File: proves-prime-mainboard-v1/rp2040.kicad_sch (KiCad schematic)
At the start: 38 parts, among them IC1 RP2040_QFN56, IC2 AZ1117CH-3.3TRG1, SW1 KMR2, SW2 KMR2, SW3 SW_SPDT, U1 W25Q128JV, Y1 12MHZ

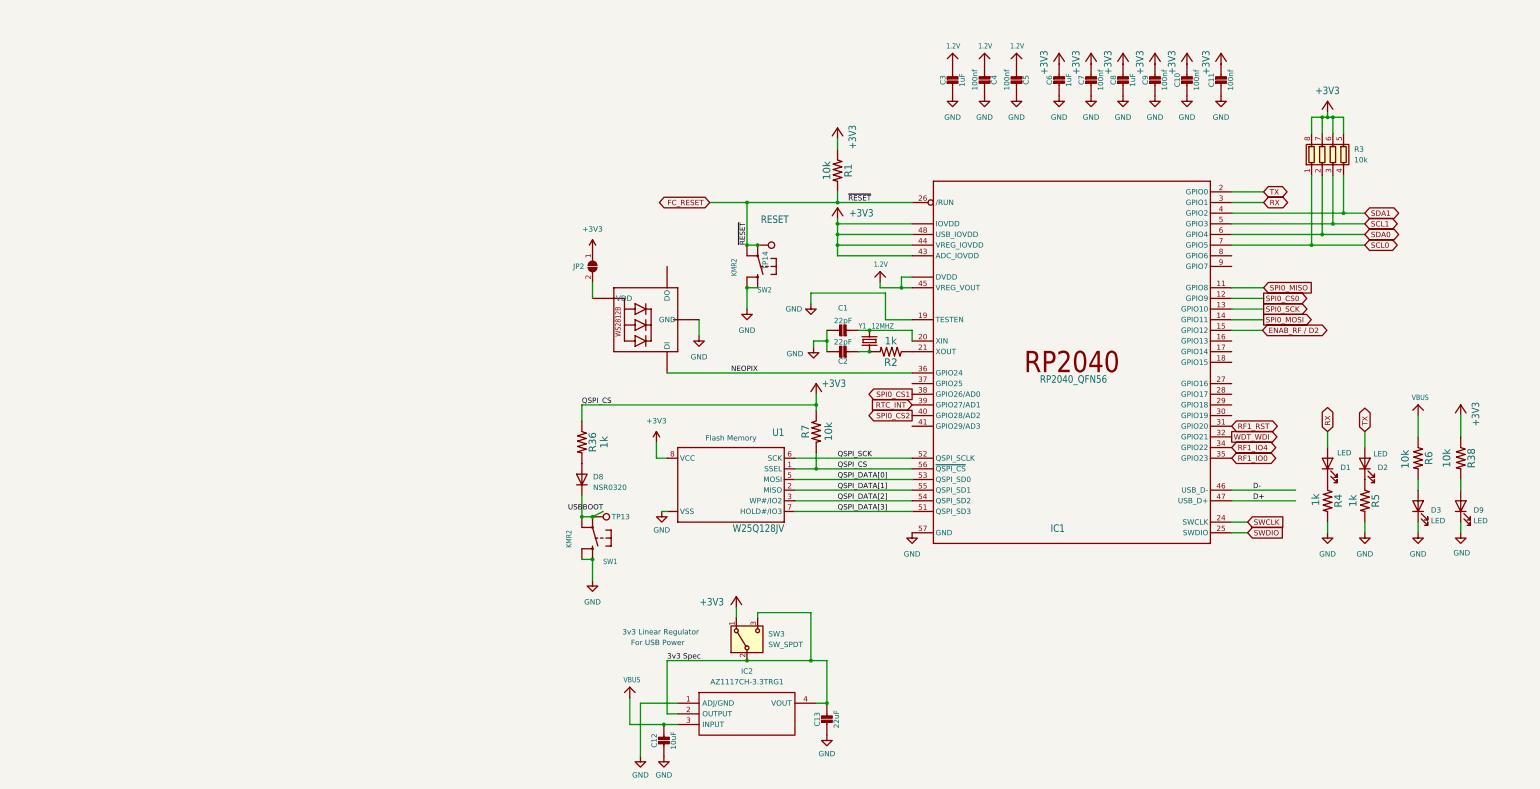
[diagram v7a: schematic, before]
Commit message: Removed RP2040
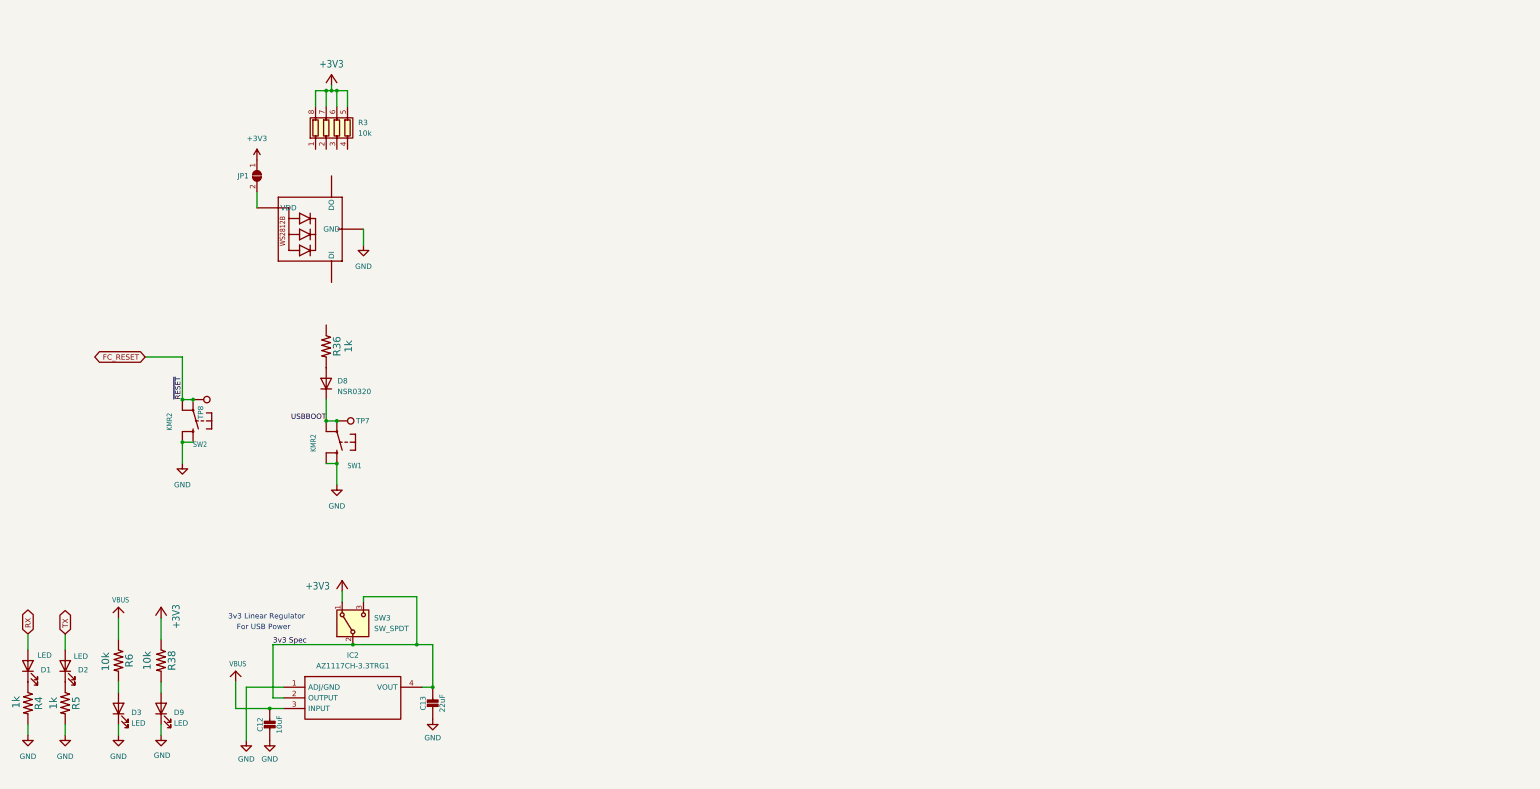
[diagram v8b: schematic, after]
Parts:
- removed C1, C2: 22pF, Capacitor_SMD:C_0402_1005Metric, symbol Adafruit ItsyBitsy RP2040-eagle-import:CAP_CERAMIC_0402NO
- removed C10, C11, C4, C5, C7, C9: 100nf, Capacitor_SMD:C_0402_1005Metric, symbol Adafruit ItsyBitsy RP2040-eagle-import:CAP_CERAMIC_0402NO
- removed C3, C6, C8: 1uF, Capacitor_SMD:C_0603_1608Metric, symbol Adafruit ItsyBitsy RP2040-eagle-import:CAP_CERAMIC_0603MP
- removed IC1: RP2040_QFN56, Package_DFN_QFN:QFN-56-1EP_7x7mm_P0.4mm_EP3.2x3.2mm_ThermalVias, symbol Adafruit ItsyBitsy RP2040-eagle-import:RP2040_QFN56
- removed JP2: SolderJumper_2_Open, Jumper:SolderJumper-2_P1.3mm_Open_RoundedPad1.0x1.5mm, symbol Jumper:SolderJumper_2_Open
- removed R1, R7: 10k, Resistor_SMD:R_0603_1608Metric, symbol mainboard:RESISTOR0603
- removed R2: 1k, Resistor_SMD:R_0402_1005Metric, symbol mainboard:RESISTOR0603
- removed TP13: USBBOOT, TestPoint:TestPoint_Loop_D1.80mm_Drill1.0mm_Beaded, symbol Connector:TestPoint
- removed TP14: RESET, TestPoint:TestPoint_Loop_D1.80mm_Drill1.0mm_Beaded, symbol Connector:TestPoint
- removed U1: W25Q128JV, Package_SO:SOIC-8_5.275x5.275mm_P1.27mm, symbol Adafruit ItsyBitsy RP2040-eagle-import:SPIFLASH_8PIN_4X4
- removed Y1: 12MHZ, Crystal:Crystal_SMD_2520-4Pin_2.5x2.0mm, symbol Adafruit ItsyBitsy RP2040-eagle-import:CRYSTAL2.5X2.0
- added JP1: SolderJumper_2_Open, Jumper:SolderJumper-2_P1.3mm_Open_RoundedPad1.0x1.5mm, symbol Jumper:SolderJumper_2_Open
- added TP7: USBBOOT, TestPoint:TestPoint_Loop_D1.80mm_Drill1.0mm_Beaded, symbol Connector:TestPoint
- added TP8: RESET, TestPoint:TestPoint_Loop_D1.80mm_Drill1.0mm_Beaded, symbol Connector:TestPoint
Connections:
- net +3V3: now also JP1.1 (A); no longer R36.1
- net FC_RESET: now also TP8.1
- net USBBOOT: now also TP7.1
- net at LED1.1 (VDD): now also JP1.2 (B)
- net NEOPIX: no longer names the net of LED1.4 (DI)
- net SCL0: no longer names the net of R3.1 (R1.1)
- net SCL1: no longer names the net of R3.3 (R3.1)
- net SDA0: no longer names the net of R3.2 (R2.1)
- net SDA1: no longer names the net of R3.4 (R4.1)
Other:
- note removed: "Flash Memory"
- note removed: "RESET"
- moved on the sheet: C12, C13, D1, D2, D3, D9, IC2, R38, R4, R5, R6, SW3
